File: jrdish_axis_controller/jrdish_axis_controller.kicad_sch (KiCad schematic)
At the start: 23 parts, among them J1 Conn_ARM_SWD_TagConnect_TC2030, SW1 DSHP04TSGER, U1 STM32G474RET6, X1 NX2016SA-16MHZ-EXS00A-CS07826

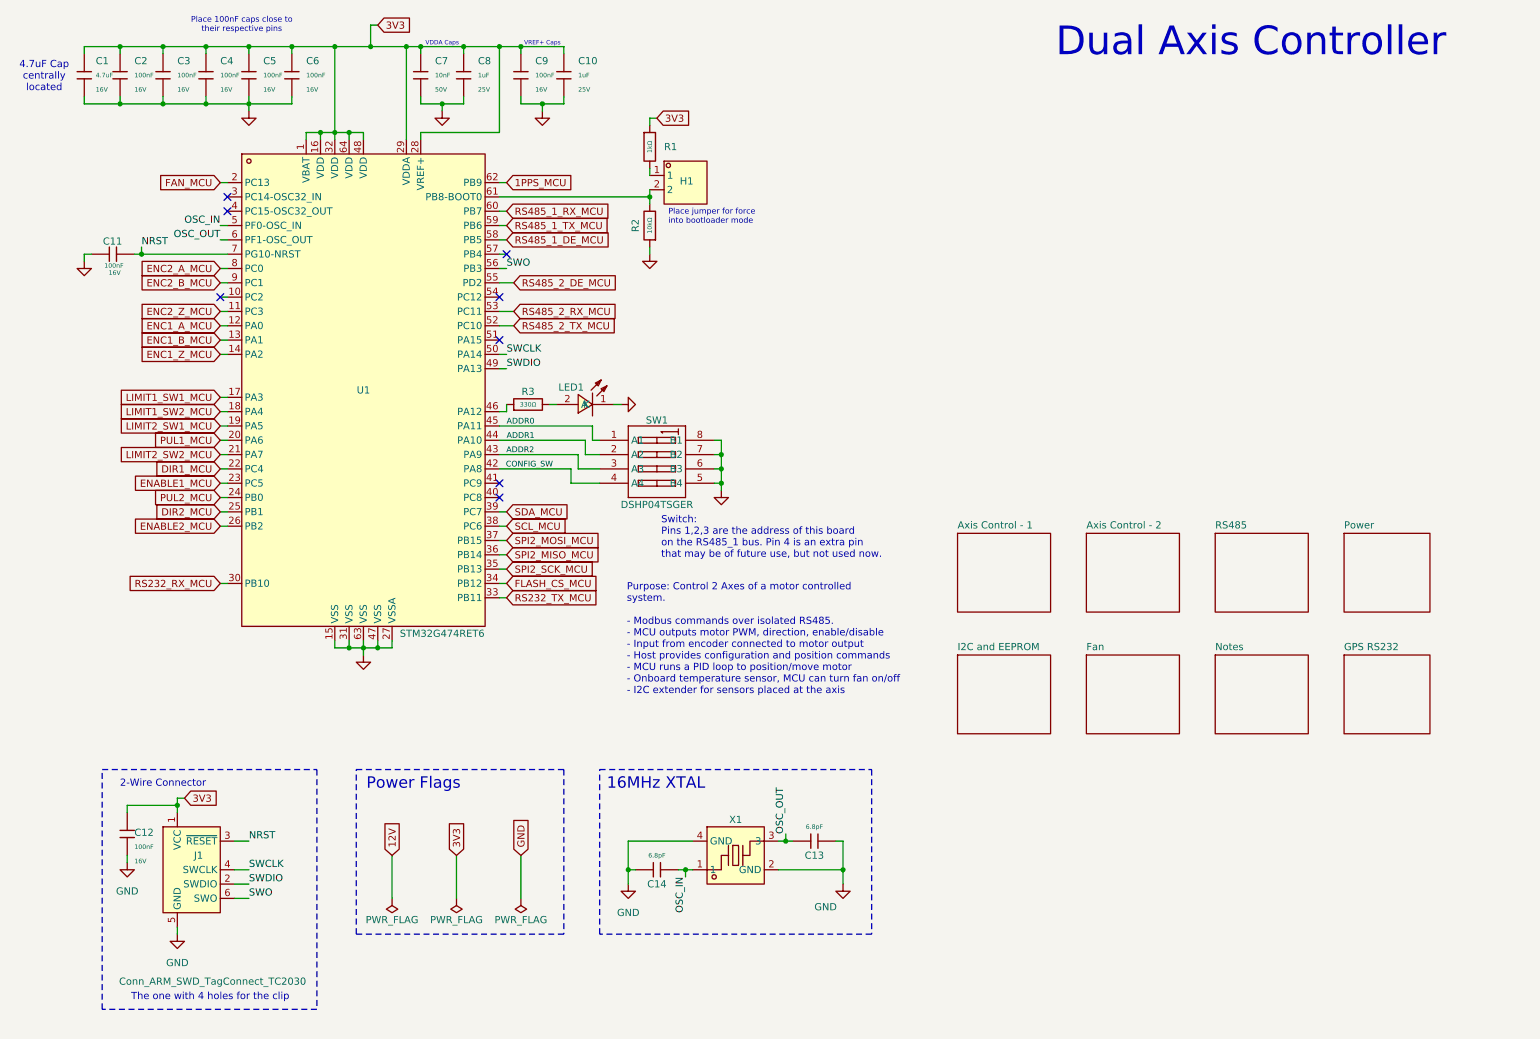
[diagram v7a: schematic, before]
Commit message: RS485 isolated areas in place
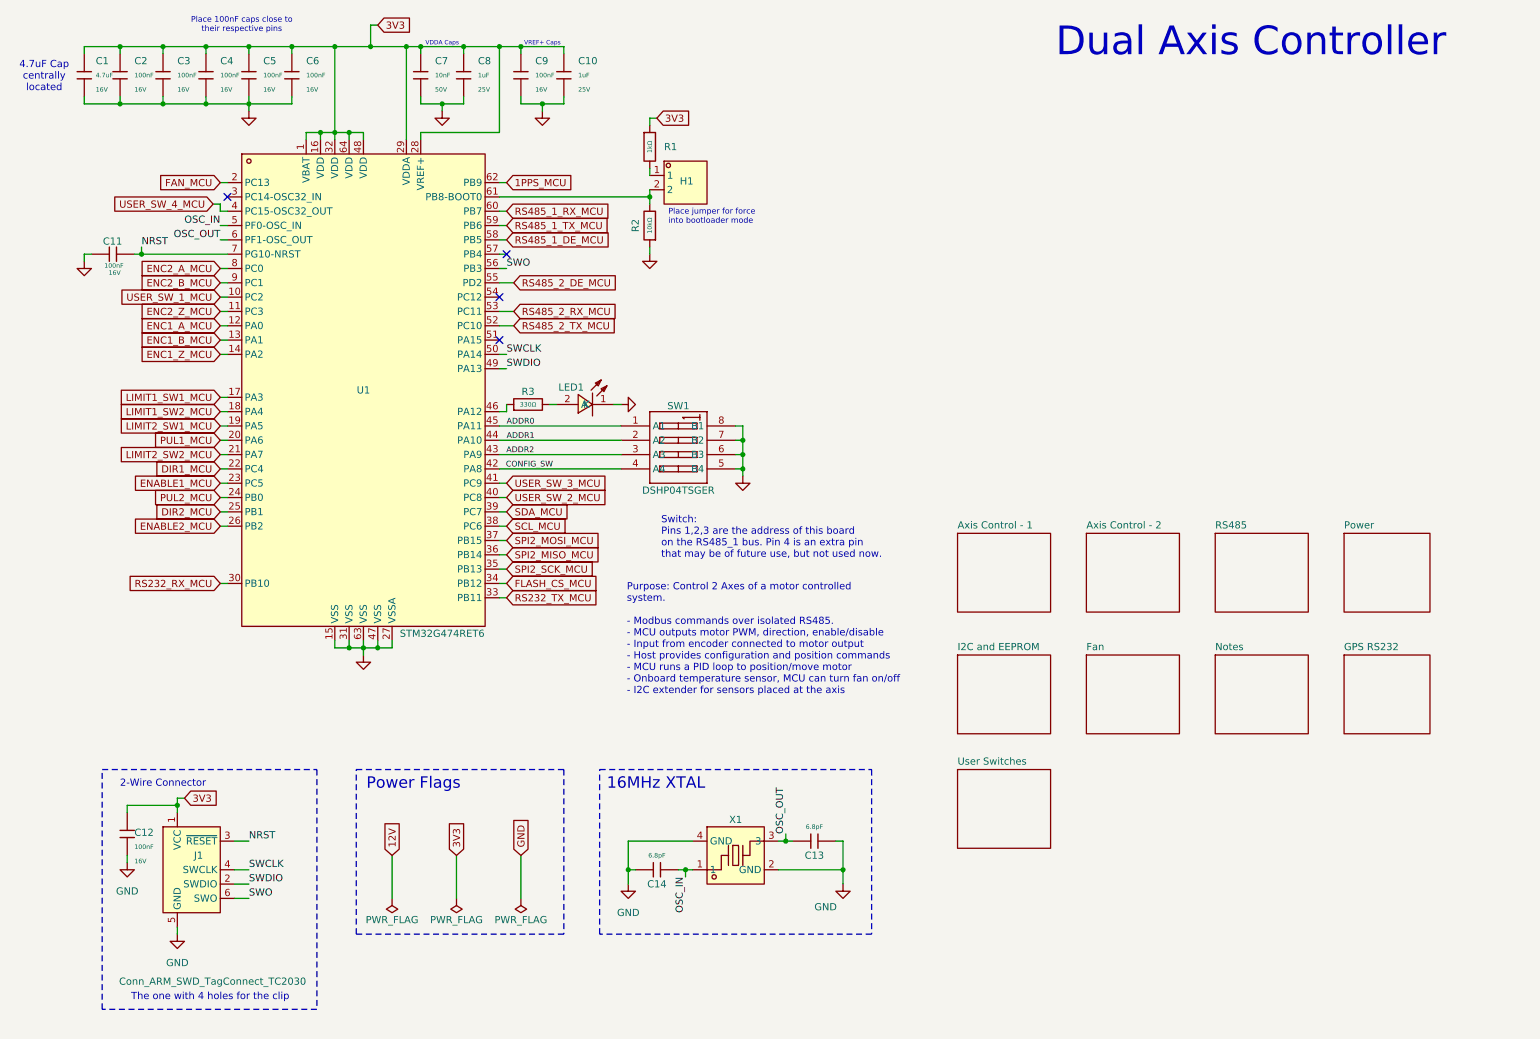
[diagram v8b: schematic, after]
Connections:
- net USER_SW_1_MCU: now reaches U1.10 (PC2)
- net USER_SW_4_MCU: now reaches U1.4 (PC15-OSC32_OUT)
- net USER_SW_2_MCU: now reaches U1.40 (PC8)
- net USER_SW_3_MCU: now reaches U1.41 (PC9)
- no-connect marks 8 -> 4
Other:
- added sheet User Switches (user_switches.kicad_sch)
- moved on the sheet: SW1
